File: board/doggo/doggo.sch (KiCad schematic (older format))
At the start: 158 parts, among them U1 IS31FL3731, U2 LIS2HH12

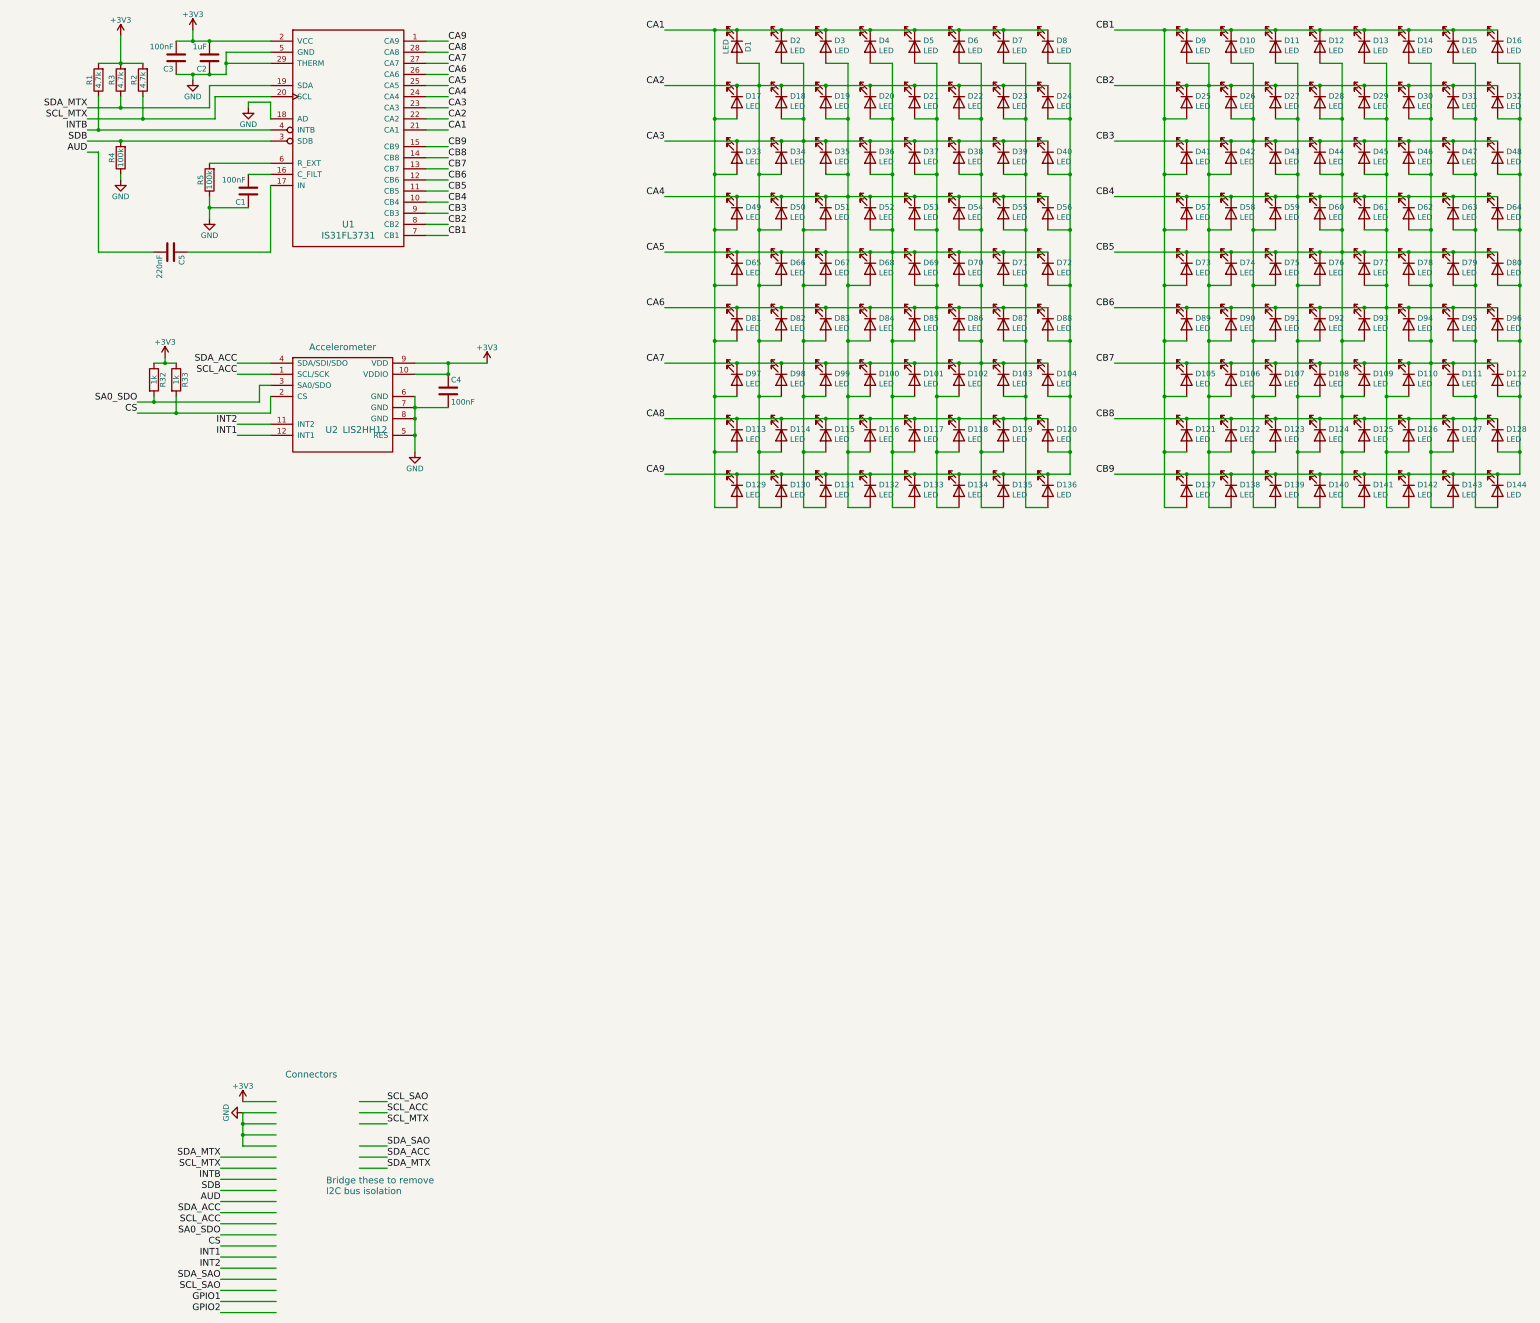
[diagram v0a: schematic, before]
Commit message: laying out LEDs
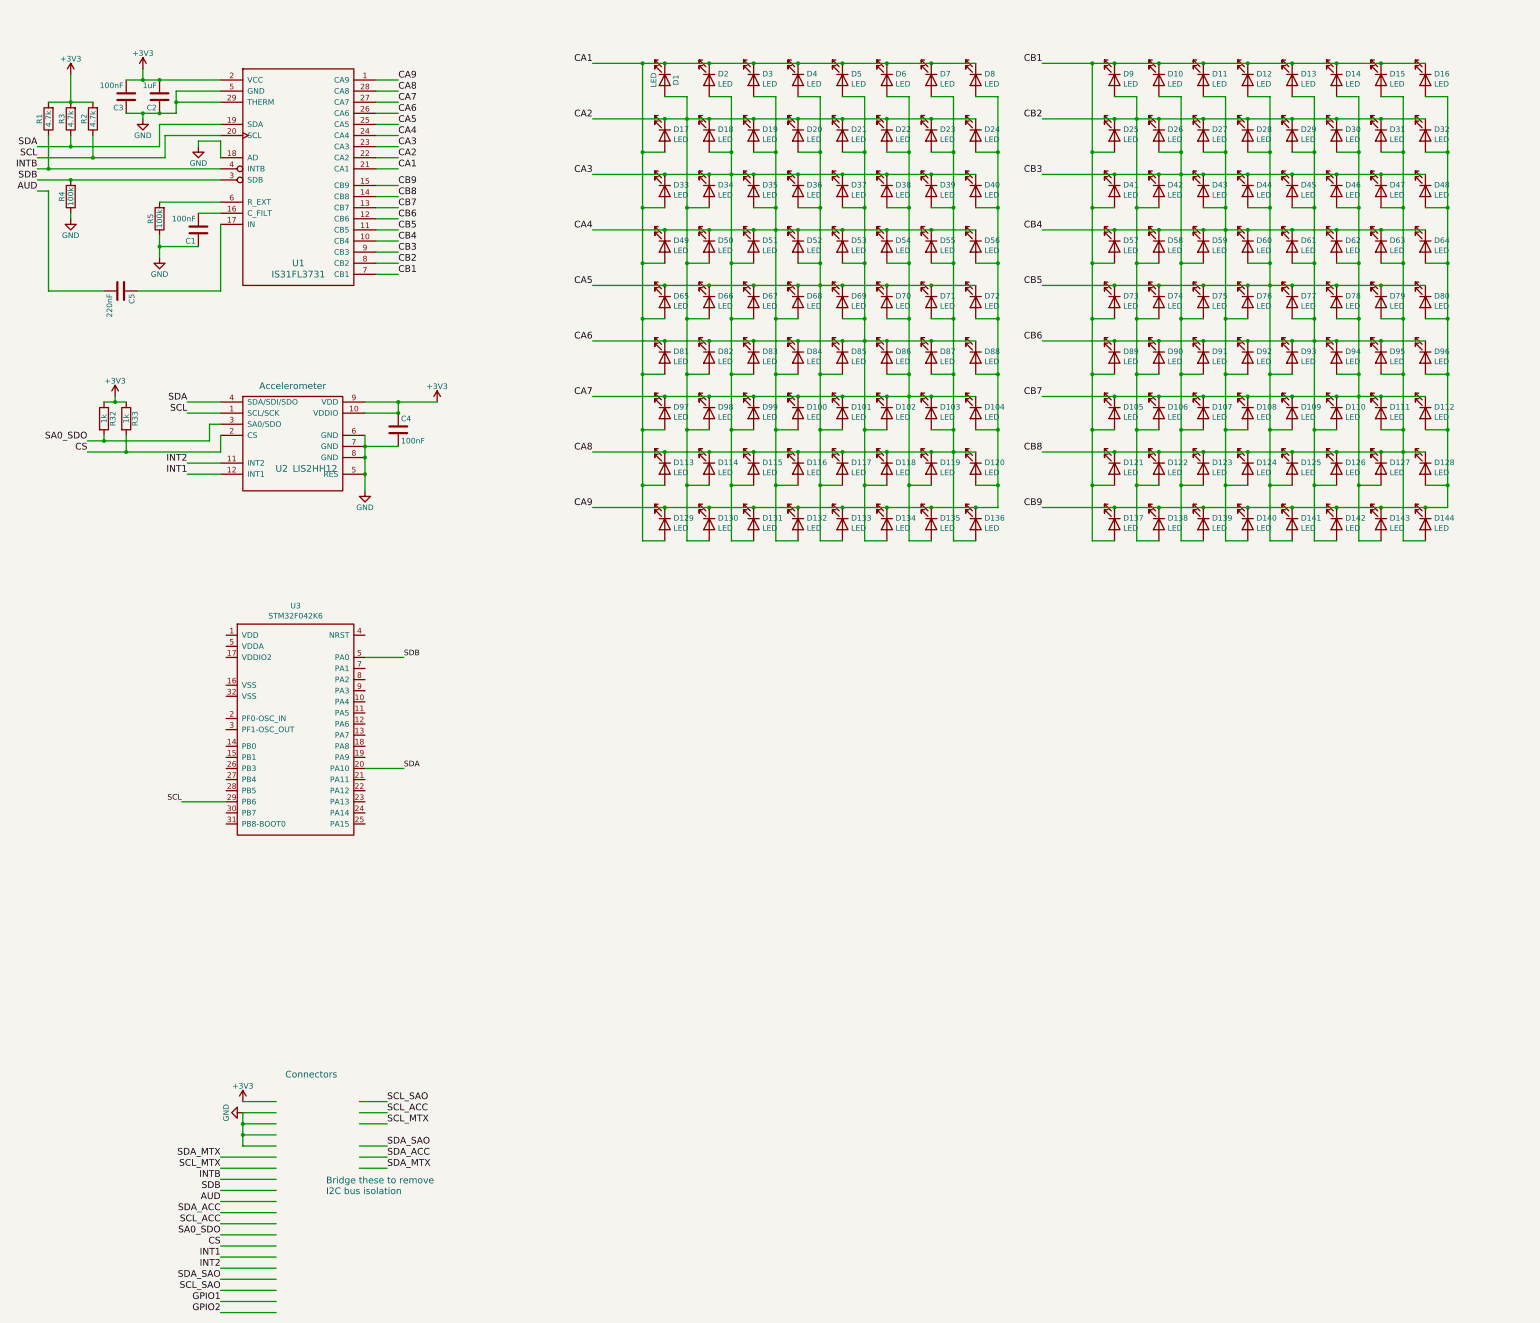
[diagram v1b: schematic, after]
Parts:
- added U3: STM32F042K6, symbol doggo:STM32F042K6
- D1: footprint LEDs:LED_0805 -> Diode_SMD:D_0402_1005Metric
- D10, D100, D101, D102, D103, D104, D105, D106, D107, D108, D109, D11, D110, D111, D112, D113, D114, D115, D116, D117, D118, D119, D12, D120, D121, D122, D123, D124, D125, D126, D127, D128, D129, D13, D130, D131, D132, D133, D134, D135, D136, D137, D138, D139, D14, D140, D141, D142, D143, D144, D15, D16, D17, D18, D19, D2, D20, D21, D22, D23, D24, D25, D26, D27, D28, D29, D3, D30, D31, D32, D33, D34, D35, D36, D37, D38, D39, D4, D40, D41, D42, D43, D44, D45, D46, D47, D48, D49, D5, D50, D51, D52, D53, D54, D55, D56, D57, D58, D59, D6, D60, D61, D62, D63, D64, D65, D66, D67, D68, D69, D7, D70, D71, D72, D73, D74, D75, D76, D77, D78, D79, D8, D80, D81, D82, D83, D84, D85, D86, D87, D88, D89, D9, D90, D91, D92, D93, D94, D95, D96, D97, D98, D99: footprint (none) -> Diode_SMD:D_0402_1005Metric
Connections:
- net labels added: SCL, SDA
- wire segments 566 -> 569
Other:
- moved on the sheet: C1, C2, C3, C4, C5, D1, D10, D100, D101, D102, D103, D104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

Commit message: worked on power support, layed out LED array
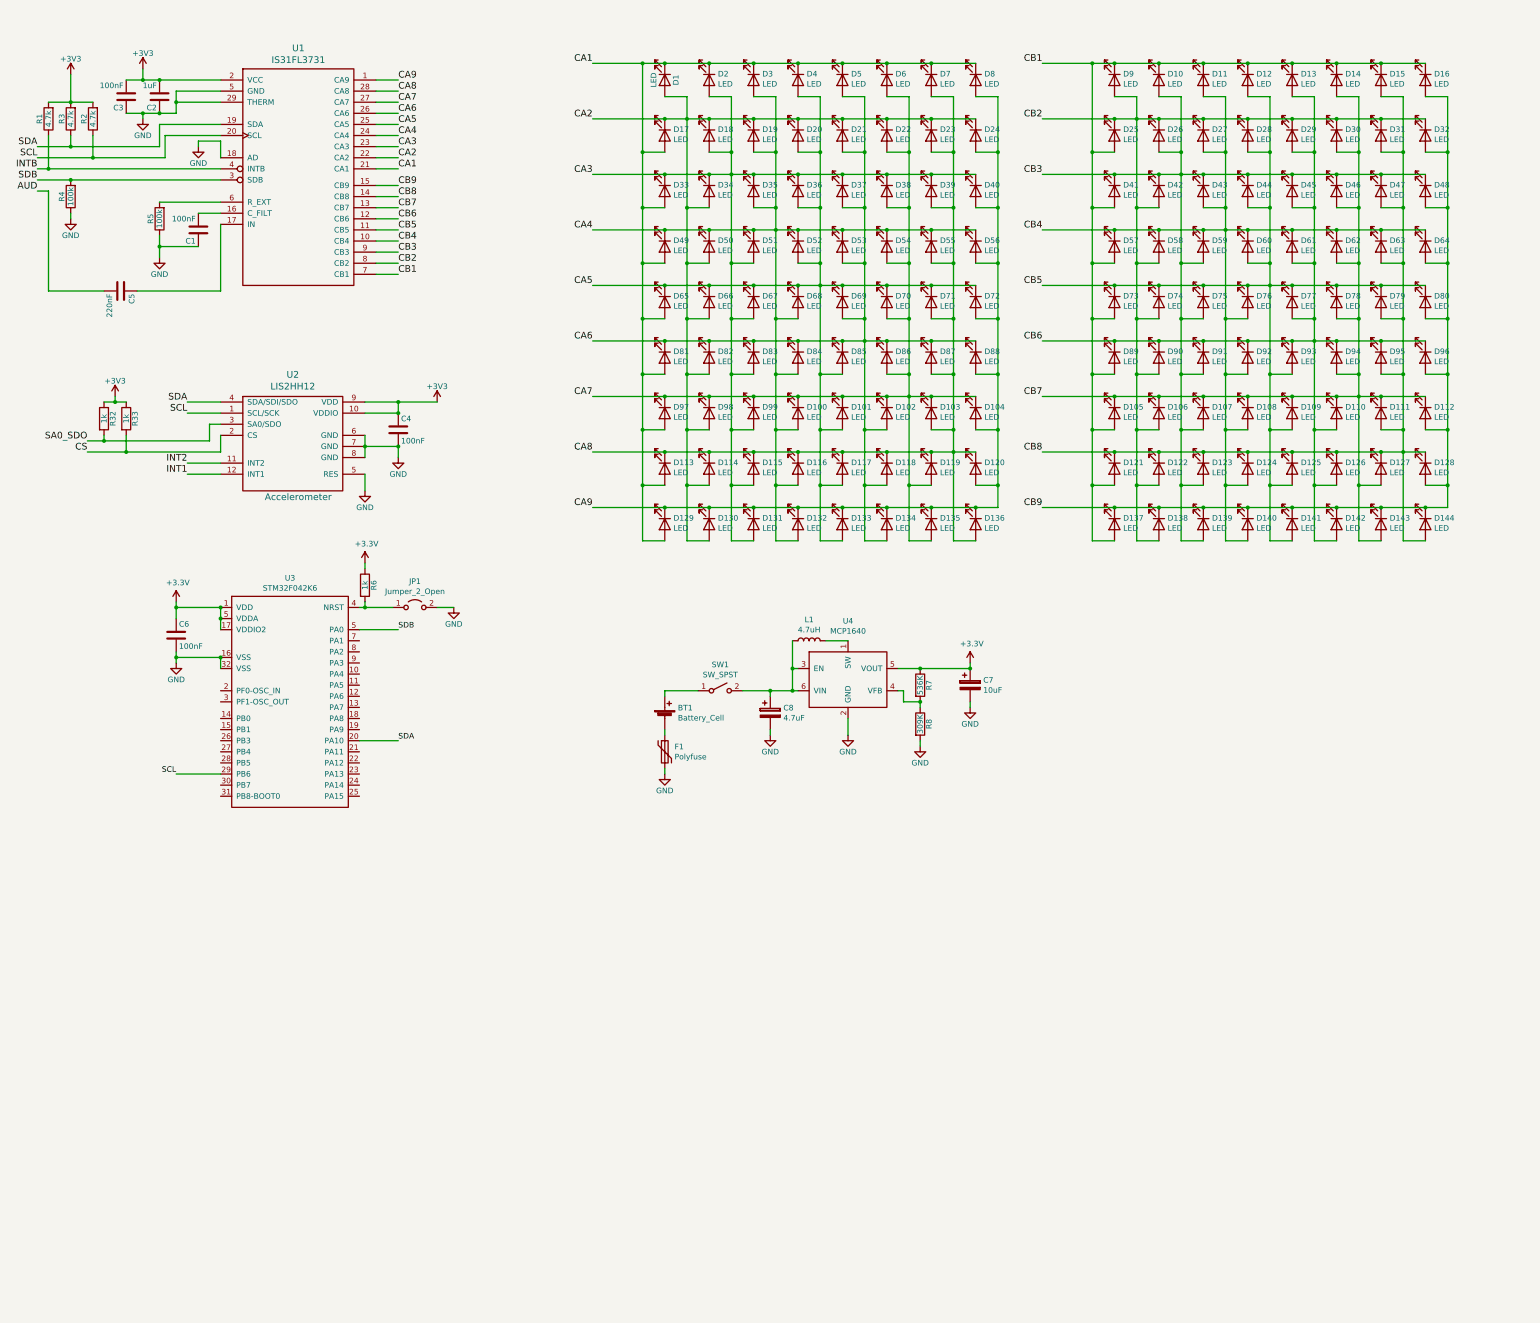
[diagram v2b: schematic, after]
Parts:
- removed U1: IS31FL3731, frkbmb:IS31FL3731C, symbol frkbmb28:IS31FL3731
- removed U2: LIS2HH12, frkbmb:LIS2HH12-NEW, symbol frkbmb28:LIS2HH12
- added BT1: Battery_Cell, symbol Device:Battery_Cell
- added C6: 100nF, Capacitor_SMD:C_0603_1608Metric, symbol Device:C
- added C7: 10uF, symbol Device:CP
- added C8: 4.7uF, symbol Device:CP
- added F1: Polyfuse, symbol Device:Polyfuse
- added JP1: Jumper_2_Open, symbol Jumper:Jumper_2_Open
- added L1: 4.7uH, symbol Device:L
- added R6: 1k, Resistor_SMD:R_0603_1608Metric, symbol Device:R
- added R7: 536K, Resistor_SMD:R_0603_1608Metric, symbol Device:R
- added R8: 309K, Resistor_SMD:R_0603_1608Metric, symbol Device:R
- added SW1: SW_SPST, symbol Switch:SW_SPST
- added U1: IS31FL3731, doggo:IS31FL3731, symbol doggo:IS31FL3731
- added U2: LIS2HH12, doggo:LIS2HH12, symbol doggo:LIS2HH12
- added U4: MCP1640, Package_TO_SOT_SMD:SOT-23-6, symbol doggo:MCP1640
- C1, C3, C4, C5: footprint Capacitors_SMD:C_0603_HandSoldering -> Capacitor_SMD:C_0603_1608Metric
- C2: footprint Capacitors_SMD:C_0805_HandSoldering -> Capacitor_SMD:C_0805_2012Metric
- R1, R2, R3, R32, R33, R4, R5: footprint Resistors_SMD:R_0603_HandSoldering -> Resistor_SMD:R_0603_1608Metric
- U3: footprint (none) -> Package_QFP:LQFP-32_7x7mm_P0.8mm
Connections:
- net labels added: +3.3V
- net labels removed: GPIO1, GPIO2, SCL_ACC, SCL_MTX, SCL_SAO, SDA_ACC, SDA_MTX, SDA_SAO
- wire segments 569 -> 577
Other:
- note removed: "Bridge these to remove\nI2C bus isolation"
- note removed: "Connectors"
- moved on the sheet: U3

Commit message: got all the footprints on the board
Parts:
- C7, C8: footprint (none) -> Capacitor_Tantalum_SMD:CP_EIA-3216-10_Kemet-I
- F1: footprint (none) -> Fuse:Fuse_1210_3225Metric
- JP1: footprint (none) -> Jumper:SolderJumper-2_P1.3mm_Open_TrianglePad1.0x1.5mm
- L1: footprint (none) -> Inductor_SMD:L_Bourns_SRN6045TA
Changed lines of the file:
@@
 F 0 "C8" H 8168 6996 50  0000 L CNN
 F 1 "4.7uF" H 8168 6905 50  0000 L CNN
-F 2 "" H 8088 6800 50  0001 C CNN
+F 2 "Capacitor_Tantalum_SMD:CP_EIA-3216-10_Kemet-I" H 8088 6800 50  0001 C CNN
 F 3 "~" H 8050 6950 50  0001 C CNN
 	1    8050 6950
@@
 F 0 "C7" H 9968 6746 50  0000 L CNN
 F 1 "10uF" H 9968 6655 50  0000 L CNN
-F 2 "" H 9888 6550 50  0001 C CNN
+F 2 "Capacitor_Tantalum_SMD:CP_EIA-3216-10_Kemet-I" H 9888 6550 50  0001 C CNN
 F 3 "~" H 9850 6700 50  0001 C CNN
 	1    9850 6700
@@
 F 0 "L1" V 8590 6300 50  0000 C CNN
 F 1 "4.7uH" V 8499 6300 50  0000 C CNN
-F 2 "" H 8400 6300 50  0001 C CNN
+F 2 "Inductor_SMD:L_Bourns_SRN6045TA" H 8400 6300 50  0001 C CNN
 F 3 "~" H 8400 6300 50  0001 C CNN
 	1    8400 6300
@@
 F 0 "F1" H 7188 7346 50  0000 L CNN
 F 1 "Polyfuse" H 7188 7255 50  0000 L CNN
-F 2 "" H 7150 7100 50  0001 L CNN
+F 2 "Fuse:Fuse_1210_3225Metric" H 7150 7100 50  0001 L CNN
 F 3 "~" H 7100 7300 50  0001 C CNN
 	1    7100 7300
@@
 F 0 "JP1" H 4850 6235 50  0000 C CNN
 F 1 "Jumper_2_Open" H 4850 6144 50  0000 C CNN
-F 2 "" H 4850 6000 50  0001 C CNN
+F 2 "Jumper:SolderJumper-2_P1.3mm_Open_TrianglePad1.0x1.5mm" H 4850 6000 50  0001 C CNN
 F 3 "~" H 4850 6000 50  0001 C CNN
 	1    4850 6000
